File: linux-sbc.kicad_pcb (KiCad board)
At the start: 6 copper layers, 550 parts, among them J1001 7499010121A, J101 Mini-fit Jr 5569, J1101 DM3AT-SF-PEJM5, J1201 PH1-08-UA, J1202 EMI shield frame, J1203 FH12A-40S-0.5SH(55), J1301 SMA RF2-04, J201 61300211121, J202 61300211121, J203 61300211121, J204 61300211121, J205 61300211121, J206 61300211121, J207 61300211121, J208 61300211121, J301 61300211121, J302 61300211121, J303 EMI shield frame, J401 EMI shield frame, J701 USB4105-GF-A, J702 TC2050-NL, J901 AU-Y1008-2-BLK, J902 AU-Y1008-2-BLK, Q201 DMPH4029LFGQ, Q202 DMPH4029LFGQ, Q203 DMN65D8L, Q204 DMPH4029LFGQ, Q205 DMPH4029LFGQ, SW501 JS202011CQN, U1001 LAN8742A-CZ-TR, U1201 TCA9554PW, U1202 AP5725FDCG-7, U1301 LBEE5KL1YN-814, U201 LM4040-5.0, U202 TL331, U203 OPA197, U204 LM4040-5.0, U205 TL331, U206 LM4040-5.0, U207 TL331, U301 AP64500SP-13, U302 AP64500SP-13, U401 STPMIC1DPQR, U501 STM32MP135FAE7, U701 FT231XQ-R, U702 TCA9554PW, U801 MT41K256M16TW, U901 USB2514B/M2, U902 AP22966DC8-7, U903 AP22966DC8-7, Y501 32.768 kHz, Y502 24 MHz, Y901 24 MHz

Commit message: Add and use a better ARGB footprint
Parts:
- D704, D707: footprint LED_SMD:LED_RGB_Wuerth-PLCC4_3.2x2.8mm_150141M173100 -> linux-sbc:LED_RGB_Wuerth-PLCC4_3.2x2.8mm_150141M173100
- moved R212 0.22 mm to (-271.1, -187.7)
- moved R211 0.10 mm to (-269.5, -187.1)
- moved C206 0.10 mm to (-271.1, -186.5)

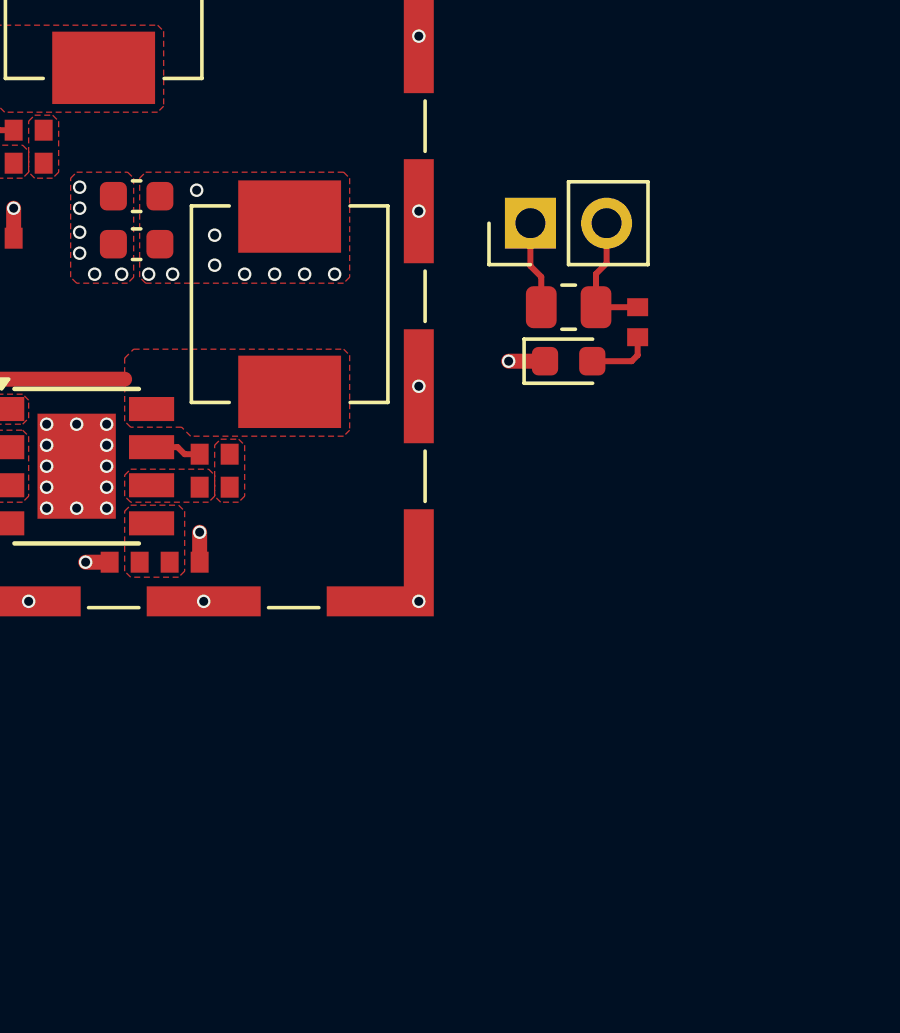
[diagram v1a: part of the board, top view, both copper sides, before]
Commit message: Remove DRC markers
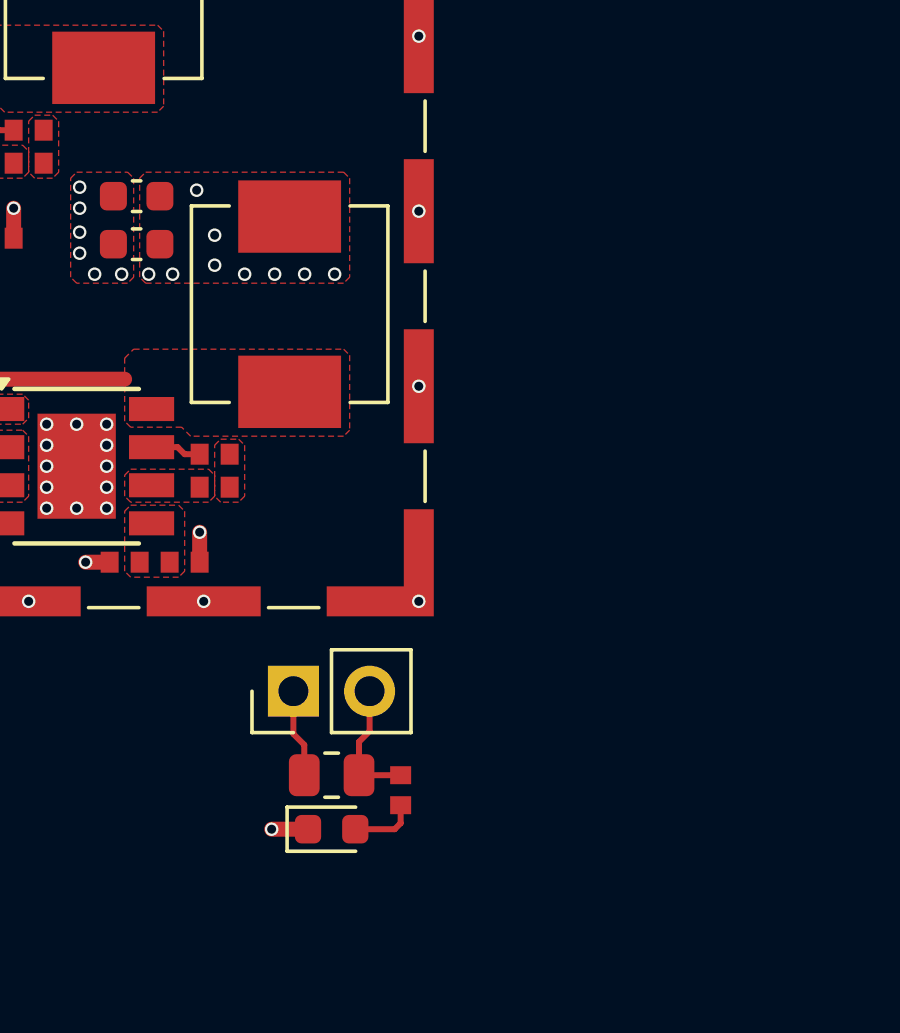
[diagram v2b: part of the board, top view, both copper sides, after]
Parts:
- moved R312 17.5 mm to (-271.6, -127.7)
- moved J302 17.5 mm to (-275.2, -131.0)
- moved R311 17.5 mm to (-273.9, -128.2)
- moved D302 17.5 mm to (-273.9, -126.4)
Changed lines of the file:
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@@
 	(footprint "perfect_footprints:R_0402_1005Metric_HDI"
 		(layer "F.Cu")
-		(at -263.7 -143.3 -90)
+		(at -271.6 -127.7 -90)
 		(property "Reference" "R312"
 			(at 0 -1.099999 270)
@@
 	(footprint "Resistor_SMD:R_0805_2012Metric"
 		(layer "F.Cu")
-		(at -266 -143.8)
+		(at -273.9 -128.2)
 		(descr "Resistor SMD 0805 (2012 Metric), square (rectangular) end terminal, IPC-7351 nominal, (Body size source: IPC-SM-782 page 72, https://www.pcb-3d.com/wordpress/wp-content/uploads/ipc-sm-782a_amendment_1_and_2.pdf), generated with kicad-footprint-generator")
 		(tags "resistor")
@@
 	(footprint "Connector_PinHeader_2.54mm:PinHeader_1x02_P2.54mm_Vertical"
 		(layer "F.Cu")
-		(at -267.275 -146.6 90)
+		(at -275.175 -131 90)
 		(descr "Through hole straight pin header, 1x02, 2.54mm pitch, single row")
 		(tags "Through hole pin header THT 1x02 2.54mm single row")
@@
 	(footprint "LED_SMD:LED_0603_1608Metric"
 		(layer "F.Cu")
-		(at -266 -142)
+		(at -273.9 -126.4)
 		(descr "LED SMD 0603 (1608 Metric), square (rectangular) end terminal, IPC-7351 nominal, (Body size source: http://www.tortai-tech.com/upload/download/2011102023233369053.pdf), generated with kicad-footprint-generator")
 		(tags "LED")
@@
 	)
 	(segment
-		(start -266.787501 -142)
-		(end -268 -142)
+		(start -274.687501 -126.4)
+		(end -275.9 -126.4)
 		(width 0.5)
 		(layer "F.Cu")
@@
 	)
 	(via
-		(at -268 -142)
+		(at -275.9 -126.4)
 		(size 0.45)
 		(drill 0.3)
@@
 	)
 	(segment
-		(start -266.9125 -144.812501)
-		(end -267.275 -145.175)
+		(start -274.8125 -129.212501)
+		(end -275.175 -129.575)
 		(width 0.2)
 		(layer "F.Cu")
@@
 	)
 	(segment
-		(start -266.9125 -143.8)
-		(end -266.9125 -144.812501)
+		(start -274.8125 -128.2)
+		(end -274.8125 -129.212501)
 		(width 0.2)
 		(layer "F.Cu")
@@
 	)
 	(segment
-		(start -267.275 -145.175)
-		(end -267.275 -146.6)
+		(start -275.175 -129.575)
+		(end -275.175 -131)
 		(width 0.2)
 		(layer "F.Cu")
@@
 	)
 	(segment
-		(start -263.699999 -142.800001)
-		(end -263.7 -142.2)
+		(start -271.599999 -127.200001)
+		(end -271.6 -126.6)
 		(width 0.2)
 		(layer "F.Cu")
@@
 	)
 	(segment
-		(start -263.9 -142)
-		(end -265.212499 -142)
+		(start -271.8 -126.4)
+		(end -273.112499 -126.4)
 		(width 0.2)
 		(layer "F.Cu")
@@
 	)
 	(segment
-		(start -263.7 -142.2)
-		(end -263.9 -142)
+		(start -271.6 -126.6)
+		(end -271.8 -126.4)
 		(width 0.2)
 		(layer "F.Cu")
@@
 	)
 	(segment
-		(start -265.0875 -143.8)
-		(end -263.7 -143.799999)
+		(start -272.9875 -128.2)
+		(end -271.6 -128.199999)
 		(width 0.2)
 		(layer "F.Cu")
@@
 	)
 	(segment
-		(start -265.0875 -143.8)
-		(end -265.0875 -144.9125)
+		(start -272.9875 -128.2)
+		(end -272.9875 -129.3125)
 		(width 0.2)
 		(layer "F.Cu")
@@
 	)
 	(segment
-		(start -265.0875 -144.9125)
-		(end -264.734999 -145.265)
+		(start -272.9875 -129.3125)
+		(end -272.634999 -129.665)
 		(width 0.2)
 		(layer "F.Cu")
@@
 	)
 	(segment
-		(start -264.734999 -145.265)
-		(end -264.735 -146.6)
+		(start -272.634999 -129.665)
+		(end -272.635 -131)
 		(width 0.2)
 		(layer "F.Cu")

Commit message: Fix via sizes
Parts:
- moved C403 193.2 mm to (-302.6, 4.70), turned to -90 degrees
- moved C408 193.1 mm to (-297.0, -4.40)
- moved C407 192.7 mm to (-299.4, 5.00), turned to -90 degrees
- moved C401 192.0 mm to (-306.0, 0.60), turned to 180 degrees
- moved C405 190.1 mm to (-297.4, 4.70), turned to -90 degrees
- moved C402 189.9 mm to (-303.9, 3.80), turned to -90 degrees
- moved C406 186.1 mm to (-296.1, 3.80), turned to -90 degrees
- moved C404 185.0 mm to (-294.0, 0.20)
- moved U401 176.4 mm to (-300.0, 0.00)

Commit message: Layout the PMIC section
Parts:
- removed the C408 at (-297.0, -4.40)
- TP401: moved to B.Cu
- moved C409 307.4 mm to (-243.5, -168.4), turned to 180 degrees
- moved C408 302.4 mm to (-240.4, -166.1)
- moved C411 301.6 mm to (-240.4, -168.3)
- moved R410 299.2 mm to (-243.7, -166.4), turned to -90 degrees
- moved C410 298.7 mm to (-240.4, -167.2)
- moved C425 295.9 mm to (-253.5, -164.0), turned to -90 degrees
- moved C423 294.4 mm to (-245.4, -155.6), turned to 180 degrees
- moved C417 294.0 mm to (-245.4, -152.4), turned to 180 degrees
- moved C418 293.4 mm to (-235.3, -167.5), turned to 180 degrees
- moved C424 292.9 mm to (-251.9, -164.0), turned to -90 degrees
- moved C420 292.7 mm to (-252.6, -157.7), turned to 180 degrees
- moved C413 292.3 mm to (-245.4, -154.5), turned to 180 degrees
- moved C421 292.0 mm to (-239.7, -157.2), turned to -90 degrees
- moved C415 291.0 mm to (-239.2, -153.4)
- moved C416 289.5 mm to (-235.3, -165.9), turned to 180 degrees
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- renumbered C403 to C402, C402 to C403, C405 to C404, C404 to C405, C407 to C406, C406 to C407, C409 to C408, C410 to C409, C411 to C410, C412 to C411, C413 to C412, C414 to C413, C415 to C414, C416 to C415, C417 to C416, C418 to C417, C419 to C418, C420 to C419, C421 to C420, C422 to C421, C423 to C422, C424 to C423, C425 to C424, C426 to C425
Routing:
- net V_5V0: track 13.1 -> 32.9 mm, vias 10 -> 20
- net /Debug/VDD: track 0.00 -> 17.6 mm, vias 0 -> 5
- net /PMIC/VDD_SD: track 0.00 -> 8.90 mm, vias 0 -> 1
- net /PMIC/PONKEY_N: track 0.00 -> 7.40 mm, vias 0 -> 1
- net /MPU/VDD_SD_IO: track 0.00 -> 6.93 mm, vias 0 -> 1
- net /PMIC/SCL: track 0.00 -> 6.54 mm, vias 0 -> 1
- net /DDR/VDD_DDR: track 0.00 -> 6.33 mm, vias 0 -> 4
- net /DDR/VREF_DDR: track 0.00 -> 6.17 mm, vias 0 -> 1
- net /MPU/VDD_CPU: track 0.00 -> 6.11 mm, vias 0 -> 4
- net /MPU/VDD_CORE: track 0.00 -> 5.94 mm, vias 0 -> 5
- net /PMIC/VDD_LDO6: track 0.00 -> 5.43 mm
- net GND: track 26.0 -> 31.2 mm, vias 131 -> 172
- net /PMIC/WAKEUP: track 0.00 -> 4.71 mm, vias 0 -> 1
- net /PMIC/INTLDO: track 0.00 -> 4.65 mm
- net /PMIC/SDA: track 0.00 -> 4.65 mm, vias 0 -> 1
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- added copper zone on F.Cu, net /DDR/VDD_DDR
- added copper zone on F.Cu, net /Debug/VDD
- added copper zone on F.Cu, net /MPU/VDD_ADC
- added copper zone on F.Cu, net /MPU/VDD_CORE
- added copper zone on F.Cu, net /MPU/VDD_CPU
- added copper zone on F.Cu, net /PMIC/VLX1
- added copper zone on F.Cu, net /PMIC/VLX2
- added copper zone on F.Cu, net /PMIC/VLX3
- added copper zone on F.Cu, net /PMIC/VLX4
